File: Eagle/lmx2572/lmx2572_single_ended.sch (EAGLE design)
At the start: 36 parts

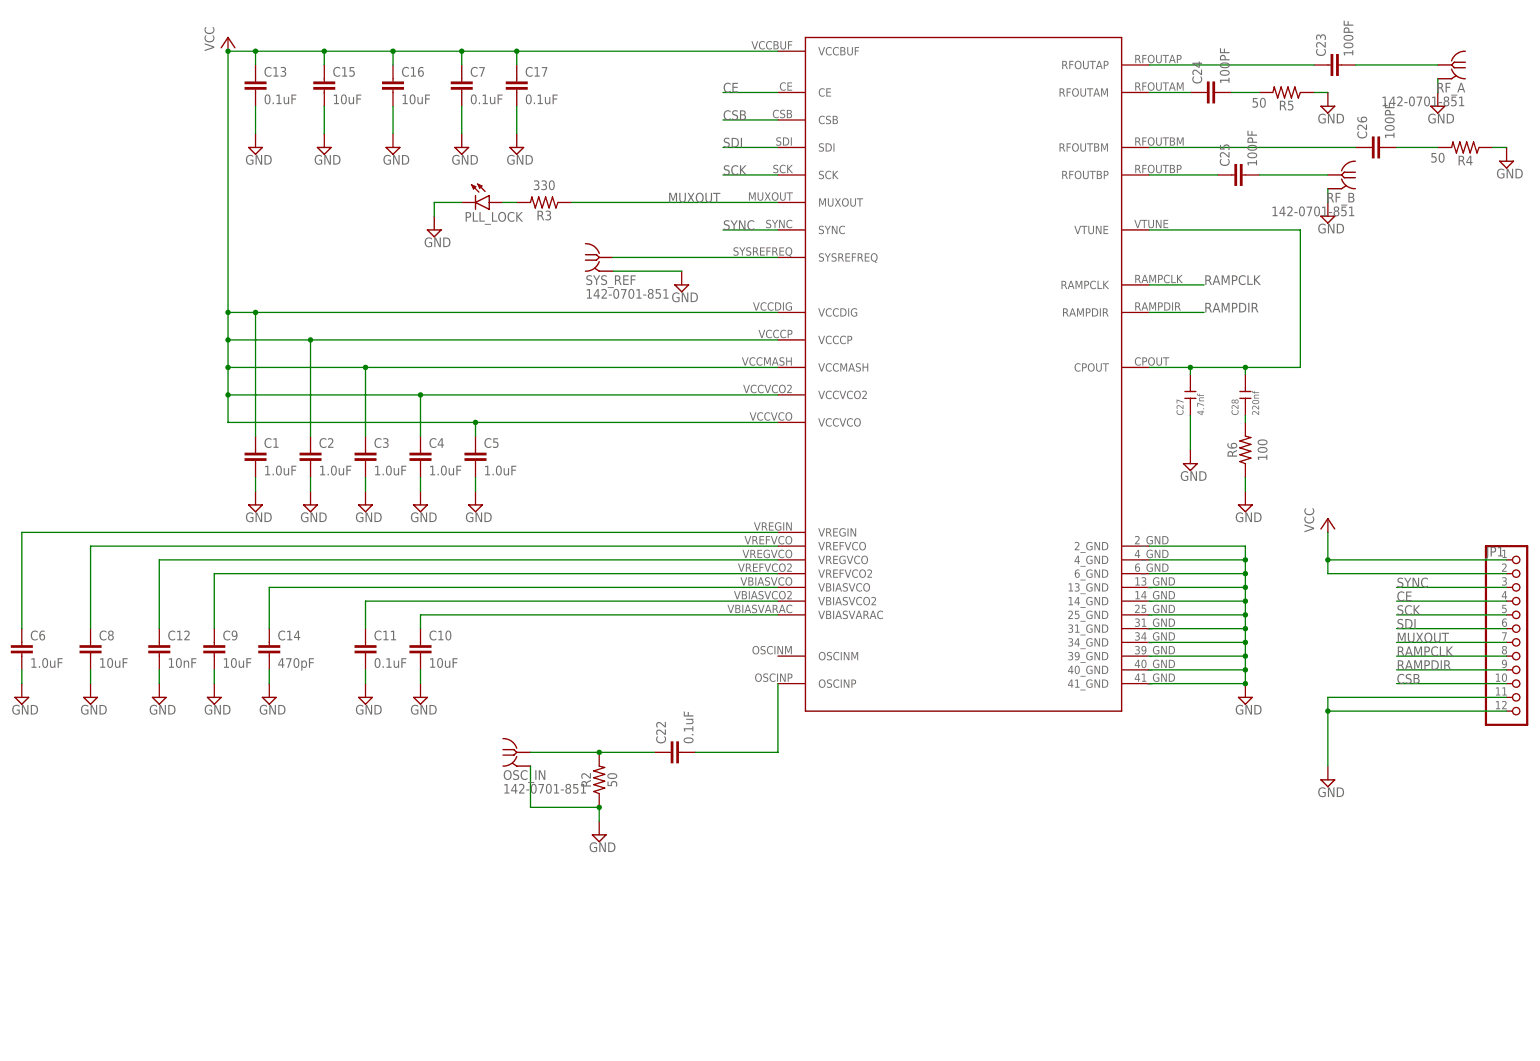
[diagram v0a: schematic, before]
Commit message: added TCXO
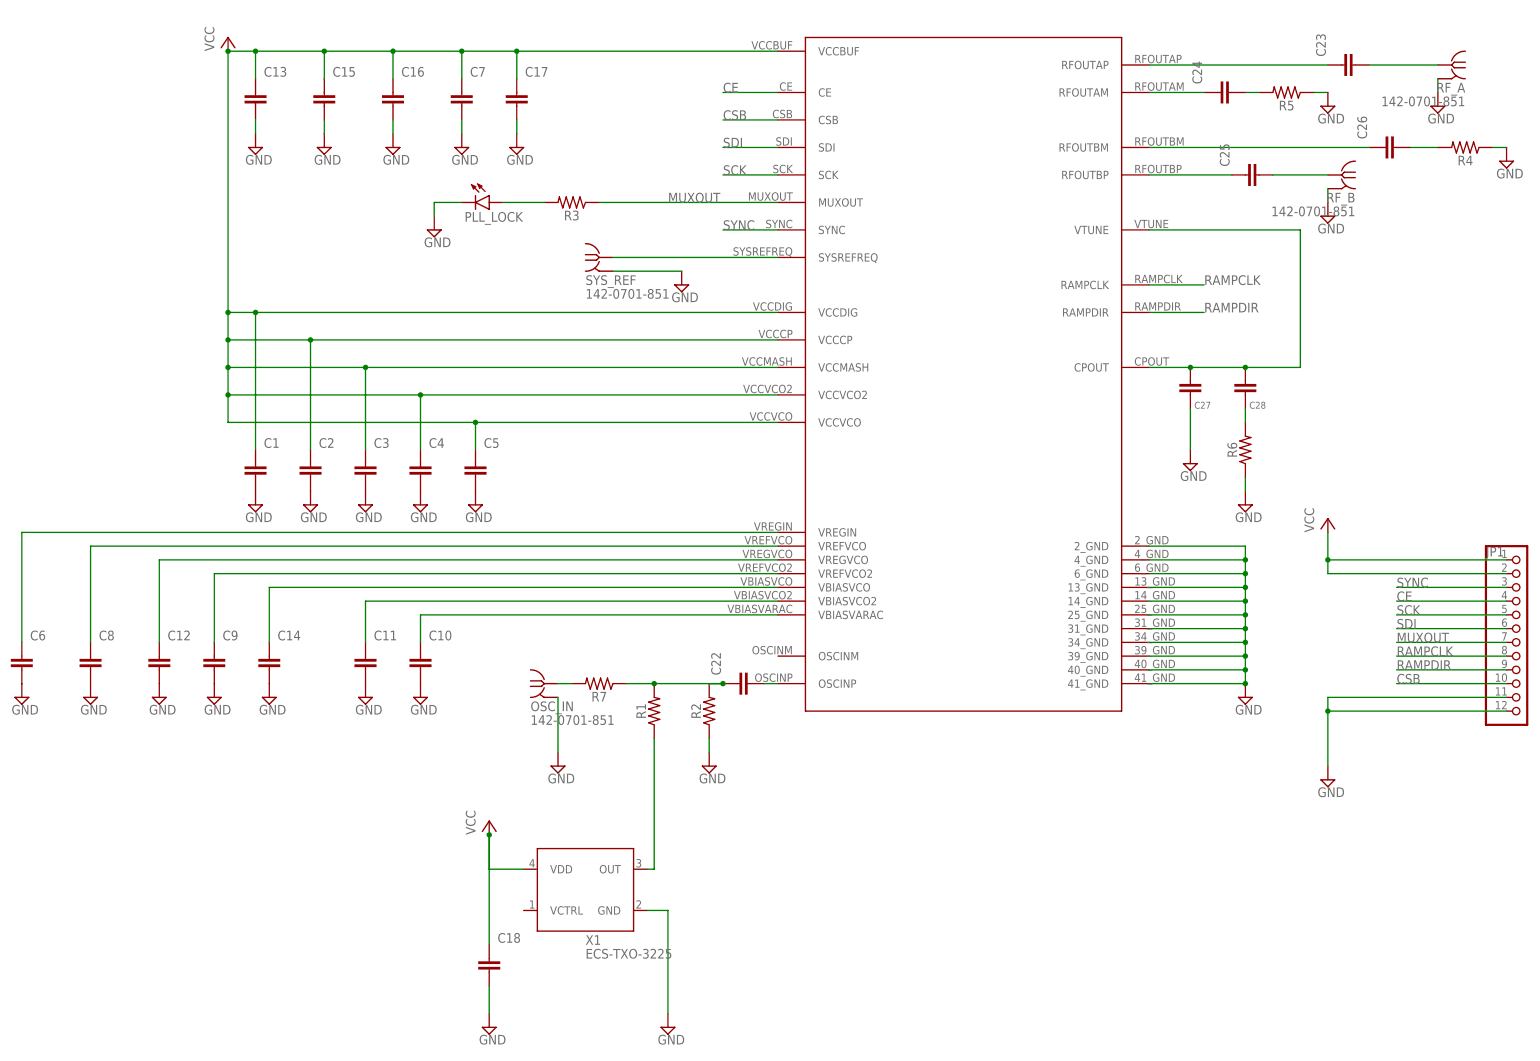
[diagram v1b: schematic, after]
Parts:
- added C18: 10uF, oresat-rcl:C-EU0603-B-NOSILK
- added R1, R7: 0, oresat-rcl:R-US_0402-C-NOSILK
- added X1: ECS-TXO-3225, X-ECS-TXO-TCXO:ECS-TXO-3225
- C1, C2, C3, C4, C5, C6: device SparkFun-Capacitors:1.0UF-0603-16V-10% -> oresat-rcl:C-EU0603-B-NOSILK
- C10, C15, C16, C8, C9: device SparkFun-Capacitors:10UF-0603-6.3V-20% -> oresat-rcl:C-EU0603-B-NOSILK
- C11, C13, C17, C7: device SparkFun-Capacitors:0.1UF-0603-25V-5% -> oresat-rcl:C-EU0603-B-NOSILK
- C12: device SparkFun-Capacitors:10NF-0603-50V-10% -> oresat-rcl:C-EU0603-B-NOSILK
- C14: device SparkFun-Capacitors:470PF-0603-50V-5% -> oresat-rcl:C-EU0603-B-NOSILK
- C22: device SparkFun-Capacitors:0.1UF-0402-16V-10% -> oresat-rcl:C-EU0402-C-NOSILK
- C23, C24, C25, C26: device SparkFun-Capacitors:100PF-0402-50V-5% -> oresat-rcl:C-EU0402-C-NOSILK
- C27: device OPL_Capacitor:CERAMIC-4.7NF-50V-10%-X7R(0603) -> oresat-rcl:C-EU0402-C-NOSILK
- C28: device OPL_Capacitor:CERAMIC-220NF-25V-10%-X7R(0603) -> oresat-rcl:C-EU0402-C-NOSILK
- R2: device SparkFun-Resistors:RESISTOR0603 -> oresat-rcl:R-US_0402-C-NOSILK; PROD_ID 50 -> (none)
- R3: device SparkFun-Resistors:RESISTOR0603 -> oresat-rcl:R-US_0603-B-NOSILK
- R4, R5, R6: device SparkFun-Resistors:RESISTOR0603 -> oresat-rcl:R-US_0402-C-NOSILK
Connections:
- new net N$11: OSC_IN.RF, R7.2
- new net N$21: C22.1, R1.2, R2.2, R7.1
- net GND: now also C18.2, X1.GND
- net N$9: now also R1.1, X1.OUT; no longer C22.1, OSC_IN.RF, R2.2
- net VCC: now also C18.1, X1.VDD
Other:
- moved on the sheet: OSC_IN

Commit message: review and updates before sending it to oshpark
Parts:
- added PWR: (no value), led:LEDCHIP-LED0603
- added R8: 0, oresat-rcl:R-US_0402-C-NOSILK
- added R9: 330, oresat-rcl:R-US_0603-B-NOSILK
- renumbered PLL_LOCK to PLL
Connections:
- new net N$10: R8.1, X1.VDD
- new net N$25: PWR.A, R9.1
- net GND: now also PWR.C
- net VCC: now also R8.2, R9.2; no longer X1.VDD
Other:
- moved on the sheet: C18
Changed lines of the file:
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@@
 <part name="SYS_REF" library="J-Cinch-142-0701-851-SMA-end-launch" deviceset="142-0701-851" device=""/>
 <part name="SUPPLY24" library="supply2" library_urn="urn:adsk.eagle:library:372" deviceset="GND" device=""/>
-<part name="PLL_LOCK" library="led" library_urn="urn:adsk.eagle:library:259" deviceset="LED" device="CHIP-LED0603" package3d_urn="urn:adsk.eagle:package:15819/3"/>
+<part name="PLL" library="led" library_urn="urn:adsk.eagle:library:259" deviceset="LED" device="CHIP-LED0603" package3d_urn="urn:adsk.eagle:package:15819/3"/>
 <part name="R3" library="oresat-rcl" deviceset="R-US_" device="0603-B-NOSILK" value="330"/>
 <part name="SUPPLY25" library="supply2" library_urn="urn:adsk.eagle:library:372" deviceset="GND" device=""/>
@@
 <part name="SUPPLY21" library="supply2" library_urn="urn:adsk.eagle:library:372" deviceset="GND" device=""/>
 <part name="C18" library="oresat-rcl" deviceset="C-EU" device="0603-B-NOSILK" value="10uF"/>
+<part name="R8" library="oresat-rcl" deviceset="R-US_" device="0402-C-NOSILK" value="0"/>
+<part name="PWR" library="led" library_urn="urn:adsk.eagle:library:259" deviceset="LED" device="CHIP-LED0603" package3d_urn="urn:adsk.eagle:package:15819/3"/>
+<part name="R9" library="oresat-rcl" deviceset="R-US_" device="0603-B-NOSILK" value="330"/>
+<part name="P+4" library="supply1" library_urn="urn:adsk.eagle:library:371" deviceset="VCC" device=""/>
+<part name="SUPPLY23" library="supply2" library_urn="urn:adsk.eagle:library:372" deviceset="GND" device=""/>
 </parts>
 <sheets>
@@
 <attribute name="VALUE" x="155.575" y="182.245" size="1.778" layer="96"/>
 </instance>
-<instance part="PLL_LOCK" gate="G$1" x="121.92" y="200.66" smashed="yes" rot="R270">
+<instance part="PLL" gate="G$1" x="121.92" y="200.66" smashed="yes" rot="R270">
 <attribute name="NAME" x="117.348" y="197.104" size="1.778" layer="95"/>
 <attribute name="VALUE" x="117.348" y="194.945" size="1.778" layer="96"/>
@@
 <attribute name="VALUE" x="153.035" y="45.085" size="1.778" layer="96"/>
 </instance>
-<instance part="P+3" gate="VCC" x="121.92" y="86.36" smashed="yes">
-<attribute name="VALUE" x="119.38" y="83.82" size="1.778" layer="96" rot="R90"/>
+<instance part="P+3" gate="VCC" x="104.14" y="93.98" smashed="yes">
+<attribute name="VALUE" x="101.6" y="91.44" size="1.778" layer="96" rot="R90"/>
 </instance>
 <instance part="R1" gate="R" x="152.4" y="106.68" smashed="yes" rot="R90">
@@
 <attribute name="NAME" x="142.24" y="110.236" size="1.778" layer="95" font="vector" rot="R180" align="bottom-center"/>
 </instance>
-<instance part="SUPPLY21" gate="GND" x="121.92" y="48.26" smashed="yes">
-<attribute name="VALUE" x="120.015" y="45.085" size="1.778" layer="96"/>
-</instance>
-<instance part="C18" gate="CE" x="121.92" y="60.96" smashed="yes">
-<attribute name="NAME" x="123.444" y="63.881" size="1.778" layer="95" font="vector"/>
+<instance part="SUPPLY21" gate="GND" x="104.14" y="48.26" smashed="yes">
+<attribute name="VALUE" x="102.235" y="45.085" size="1.778" layer="96"/>
+</instance>
+<instance part="C18" gate="CE" x="104.14" y="58.42" smashed="yes">
+<attribute name="NAME" x="105.664" y="61.341" size="1.778" layer="95" font="vector"/>
+</instance>
+<instance part="R8" gate="R" x="109.22" y="76.2" smashed="yes" rot="R180">
+<attribute name="NAME" x="109.22" y="74.676" size="1.778" layer="95" font="vector" rot="R180" align="bottom-center"/>
+</instance>
+<instance part="PWR" gate="G$1" x="228.6" y="68.58" smashed="yes" rot="R90">
+<attribute name="NAME" x="233.172" y="72.136" size="1.778" layer="95" rot="R180"/>
+<attribute name="VALUE" x="233.172" y="74.295" size="1.778" layer="96" rot="R180"/>
+</instance>
+<instance part="R9" gate="R" x="213.36" y="68.58" smashed="yes" rot="R180">
+<attribute name="NAME" x="213.36" y="67.056" size="1.778" layer="95" font="vector" rot="R180" align="bottom-center"/>
+</instance>
+<instance part="P+4" gate="VCC" x="200.66" y="76.2" smashed="yes">
+<attribute name="VALUE" x="198.12" y="73.66" size="1.778" layer="96" rot="R90"/>
+</instance>
+<instance part="SUPPLY23" gate="GND" x="243.84" y="60.96" smashed="yes">
+<attribute name="VALUE" x="241.935" y="57.785" size="1.778" layer="96"/>
 </instance>
 </instances>
@@
 </segment>
 <segment>
-<pinref part="PLL_LOCK" gate="G$1" pin="C"/>
+<pinref part="PLL" gate="G$1" pin="C"/>
 <pinref part="SUPPLY25" gate="GND" pin="GND"/>
 <wire x1="116.84" y1="200.66" x2="111.76" y2="200.66" width="0.1524" layer="91"/>
@@
 <pinref part="C18" gate="CE" pin="2"/>
 <pinref part="SUPPLY21" gate="GND" pin="GND"/>
-<wire x1="121.92" y1="50.8" x2="121.92" y2="55.88" width="0.1524" layer="91"/>
+<wire x1="104.14" y1="50.8" x2="104.14" y2="53.34" width="0.1524" layer="91"/>
+</segment>
+<segment>
+<pinref part="PWR" gate="G$1" pin="C"/>
+<pinref part="SUPPLY23" gate="GND" pin="GND"/>
+<wire x1="233.68" y1="68.58" x2="243.84" y2="68.58" width="0.1524" layer="91"/>
+<wire x1="243.84" y1="68.58" x2="243.84" y2="63.5" width="0.1524" layer="91"/>
 </segment>
 </net>
@@
 <segment>
 <pinref part="P+3" gate="VCC" pin="VCC"/>
-<pinref part="X1" gate="G$1" pin="VDD"/>
-<wire x1="121.92" y1="83.82" x2="121.92" y2="77.47" width="0.1524" layer="91"/>
-<wire x1="121.92" y1="77.47" x2="128.27" y2="77.47" width="0.1524" layer="91"/>
+<pinref part="R8" gate="R" pin="2"/>
+<wire x1="104.14" y1="91.44" x2="104.14" y2="76.2" width="0.1524" layer="91"/>
 <pinref part="C18" gate="CE" pin="1"/>
-<wire x1="121.92" y1="83.82" x2="121.92" y2="63.5" width="0.1524" layer="91"/>
-<junction x="121.92" y="83.82"/>
+<wire x1="104.14" y1="76.2" x2="104.14" y2="60.96" width="0.1524" layer="91"/>
+<junction x="104.14" y="76.2"/>
+</segment>
+<segment>
+<pinref part="P+4" gate="VCC" pin="VCC"/>
+<pinref part="R9" gate="R" pin="2"/>
+<wire x1="200.66" y1="73.66" x2="200.66" y2="68.58" width="0.1524" layer="91"/>
+<wire x1="200.66" y1="68.58" x2="208.28" y2="68.58" width="0.1524" layer="91"/>
 </segment>
 </net>
@@
 <net name="N$14" class="0">
 <segment>
-<pinref part="PLL_LOCK" gate="G$1" pin="A"/>
+<pinref part="PLL" gate="G$1" pin="A"/>
 <pinref part="R3" gate="R" pin="2"/>
 <wire x1="124.46" y1="200.66" x2="132.08" y2="200.66" width="0.1524" layer="91"/>
@@
 </segment>
 </net>
+<net name="N$10" class="0">
+<segment>
+<pinref part="R8" gate="R" pin="1"/>
+<pinref part="X1" gate="G$1" pin="VDD"/>
+<wire x1="114.3" y1="76.2" x2="114.3" y2="77.47" width="0.1524" layer="91"/>
+<wire x1="114.3" y1="77.47" x2="128.27" y2="77.47" width="0.1524" layer="91"/>
+</segment>
+</net>
+<net name="N$25" class="0">
+<segment>
+<pinref part="R9" gate="R" pin="1"/>
+<pinref part="PWR" gate="G$1" pin="A"/>
+<wire x1="218.44" y1="68.58" x2="226.06" y2="68.58" width="0.1524" layer="91"/>
+</segment>
+</net>
